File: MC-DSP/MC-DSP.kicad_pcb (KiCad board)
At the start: 6 copper layers, 160.2 x 100 mm, 165 parts, among them J1 374385, J80 5-1634513-1, J81 5-1634513-1, J82 5-1634513-1, SW1 SW_SPDT, T1 ERRORSTS, U1 TMS320F28388DZWT, U10 ECS-2520MV-xxx-xx, U12 BU4831F-TR, U13 BU4811G-TR, U2 SBH41-NBPB-D10-ST-BK, U20 R-78E3.3-1.0, U200 FT2232HL, U201 TPD2S017, U202 USB_B, U203 AZ1117-3.3, U204 ISO7730DW, U205 ISO7730DW, U206 ISO7730DW, U207 Crystal_GND24, U21 R-78B1.2-2.0, U60 OPA365xxD, U61 OPA365xxD, U62 OPA365xxD, U63 OPA365xxD, U64 OPA365xxD, U65 MAX6126AASA, U80 OPA365xxD, U81 OPA365xxD, U82 OPA365xxD

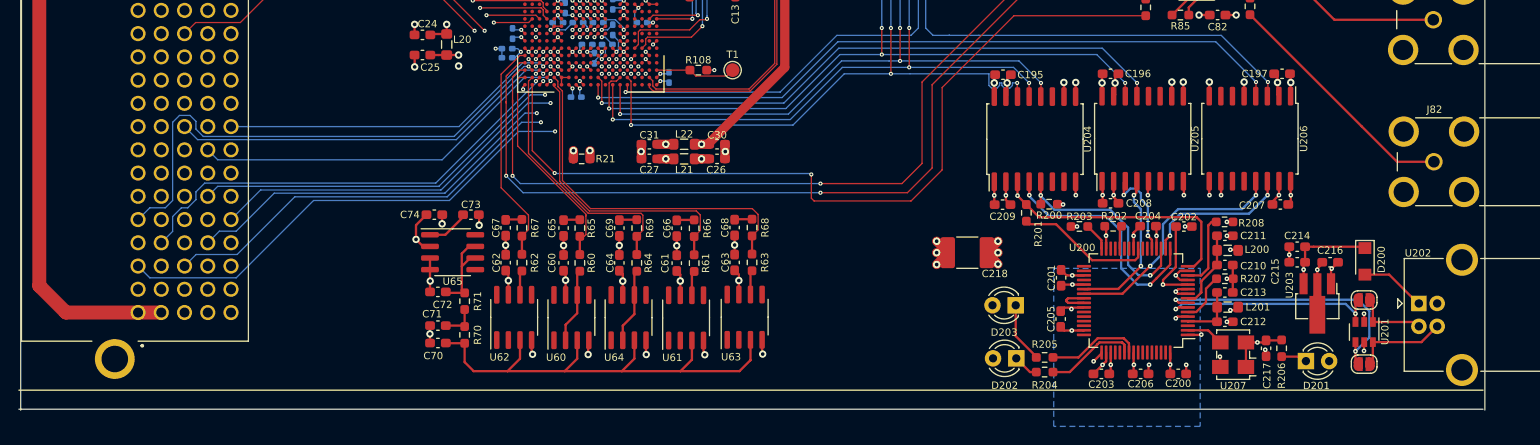
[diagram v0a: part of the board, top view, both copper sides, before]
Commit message: Fixed ADC ref low pass filter positions (moved them closer to the DSP) and fixed board outline
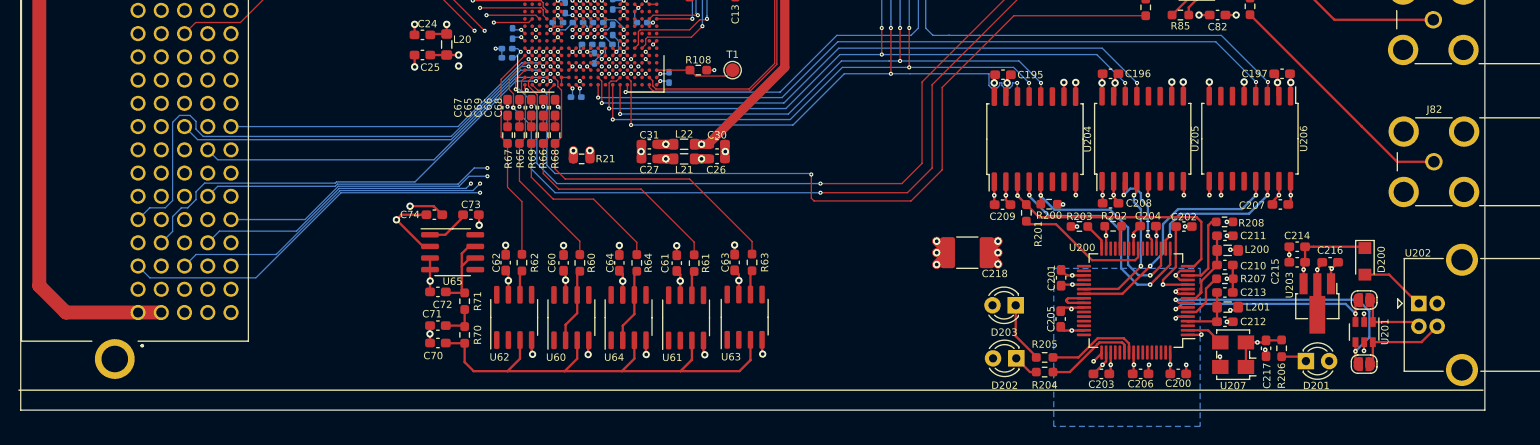
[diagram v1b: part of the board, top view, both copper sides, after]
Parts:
- moved R68 23.8 mm to (159.5, 81.7)
- moved C68 23.6 mm to (159.5, 78.7), turned to 270 degrees
- moved C66 19.7 mm to (158.2, 78.7), turned to 270 degrees
- moved R66 19.4 mm to (158.2, 81.7)
- moved C69 16.3 mm to (156.9, 78.7), turned to 270 degrees
- moved R69 15.4 mm to (156.9, 81.7)
- moved C65 14.0 mm to (155.6, 78.7), turned to 270 degrees
- moved C67 13.1 mm to (154.3, 78.7), turned to 270 degrees
- moved R65 12.1 mm to (155.6, 81.7)
- moved R67 10.3 mm to (154.3, 81.7)
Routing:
- net VDDA: track 25.5 -> 28.9 mm
- net /DAC to BNC/DAC_A: track 102.4 -> 99.2 mm
- net /DAC to BNC/DAC_B: track 101.4 -> 98.5 mm
- net /ADCrefs/HID: track 39.2 -> 36.8 mm
- net GND: track 160.4 -> 162.2 mm, vias 104 -> 109
- net /ADCrefs/HIB: track 32.3 -> 31.2 mm
- net /ADC_C4: track 46.2 -> 47.2 mm
- net /ADCrefs/HIA: track 23.7 -> 22.7 mm
- net /ADCrefs/HIC: track 24.7 -> 23.7 mm
- net /ADC_C3: track 64.7 -> 63.9 mm
- net VDAC: track 28.4 -> 27.5 mm
- net Net-(C69-Pad2): track 1.93 -> 1.22 mm
- net Net-(C66-Pad2): track 1.93 -> 1.22 mm
- net Net-(C68-Pad2): track 1.93 -> 1.22 mm
- net /ADC_D0: track 45.9 -> 46.5 mm
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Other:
- board size 160.2 x 100 mm -> 160 x 100 mm

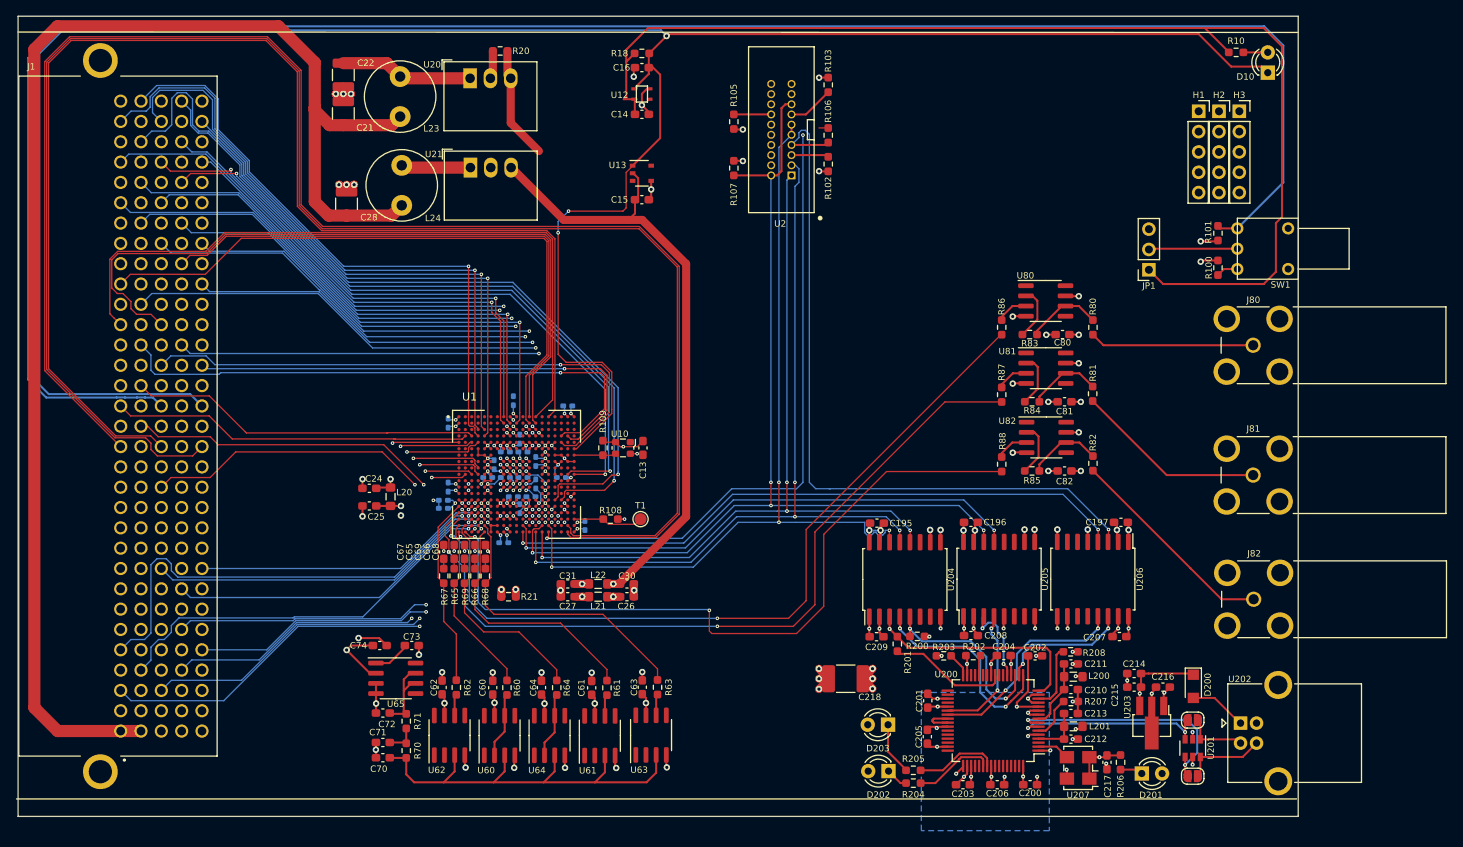
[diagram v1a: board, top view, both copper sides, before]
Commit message: Routed Last 11 tracks, fixed cu.4 gnd pour
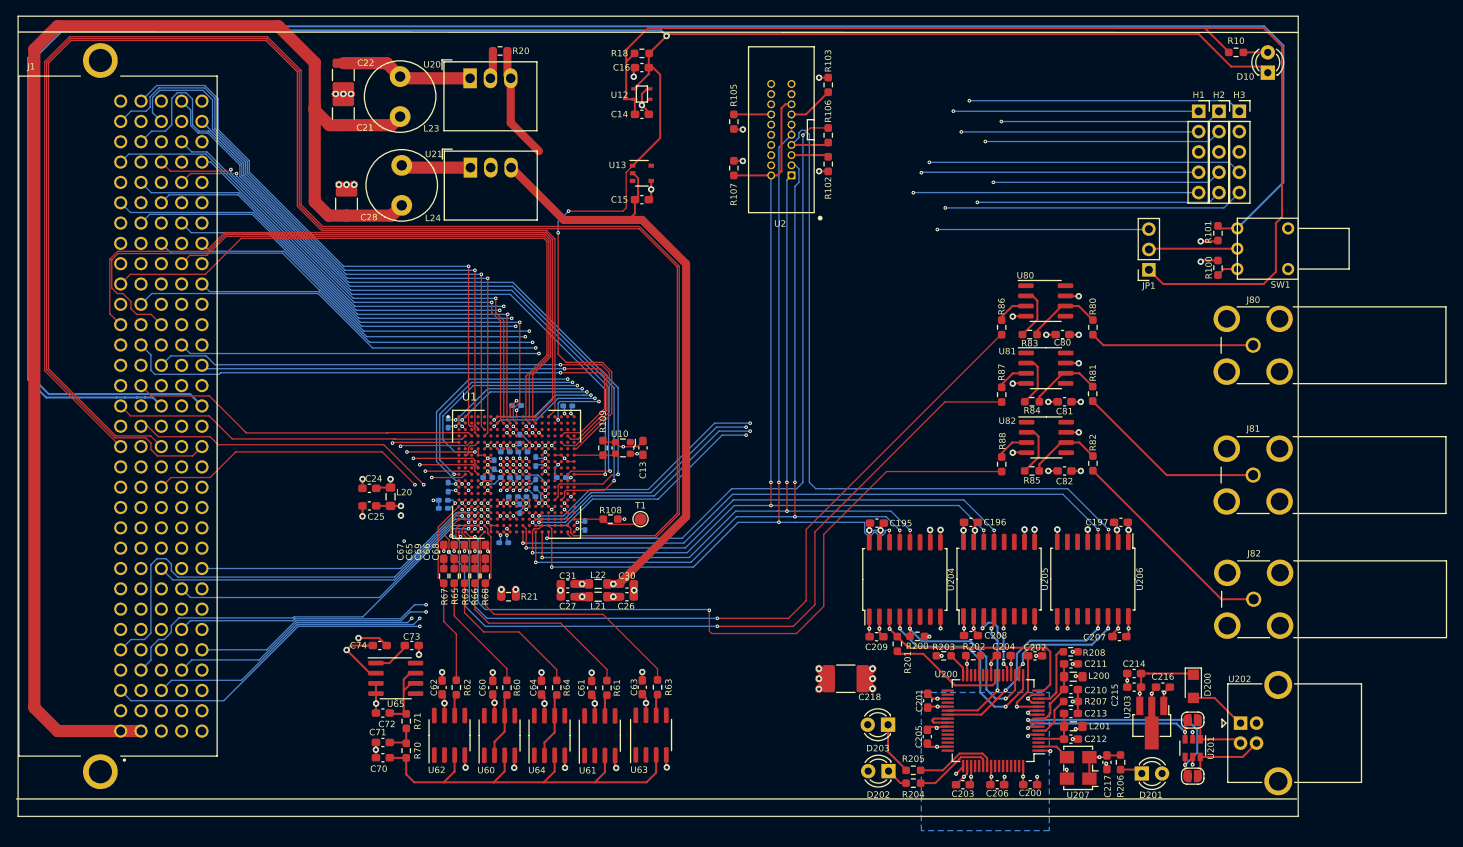
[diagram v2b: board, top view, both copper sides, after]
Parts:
- moved C188 0.72 mm to (163.4, 60.4), turned to 180 degrees
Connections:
- C80 pad 2: Net-(C80-Pad2) -> +3V3
- C81 pad 2: Net-(C80-Pad2) -> +3V3
- C82 pad 2: Net-(C80-Pad2) -> +3V3
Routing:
- net /ADCSOCAO: track 0.00 -> 131.5 mm, vias 0 -> 3
- net /OUTPUTXBAR4: track 0.00 -> 125.7 mm, vias 0 -> 3
- net /OUTPUTXBAR3: track 0.00 -> 125.2 mm, vias 0 -> 3
- net /CLB_OUTPUTX_BAR1: track 0.00 -> 116.9 mm, vias 0 -> 3
- net /OUTPUTXBAR1: track 0.00 -> 116.6 mm, vias 0 -> 3
- net /XCLKOUT: track 0.00 -> 116.0 mm, vias 0 -> 3
- net /CLB_OUTPUTX_BAR2: track 0.00 -> 114.8 mm, vias 0 -> 3
- net /ADCSOCBO: track 0.00 -> 114.8 mm, vias 0 -> 3
- net /OUTPUTXBAR2: track 0.00 -> 114.0 mm, vias 0 -> 3
- net /CLB_OUTPUTX_BAR3: track 0.00 -> 108.5 mm, vias 0 -> 3
- net /CLB_OUTPUTX_BAR4: track 0.00 -> 106.5 mm, vias 0 -> 3
- net Net-(JP1-Pad3): track 0.00 -> 102.0 mm, vias 0 -> 3
- net GND: track 162.2 -> 170.0 mm
- net /ADC_B4: track 54.9 -> 50.2 mm, vias 1 -> 2
- net VDDA: track 28.9 -> 33.3 mm
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- added copper zone on In4.Cu, net EMU_GND
- added copper zone on In4.Cu, net GND
